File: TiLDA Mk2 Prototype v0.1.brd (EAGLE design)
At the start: 67.9 x 100 mm, 199 parts, among them IC1 ATSAM3X8EA-AU, IC10 MCP73831, IC2 MPU-6050, IC3 SRF-V1.2, IC5 S25FL216K0PMFI011, IC7 HMC5883LSMD (NP), IC8 MCP1825T-3302E/DC, IC9 TC1015-3V3, J1 ZX62-AB-5PA(11), J3 Arduino Headers, J5 1050270001 (NP), J6 B016 - PowerPOD NCP1402 5V0, J7 SFV30R-2STE1HLF, J8 1x02 RA Pin, Q10 2N7002KW, Q11 BSS84W, Q12 2N7002KW, Q13 BSS84W, Q8 BSS84W, Q9 2N7002KW, U2 JHD12864-G13BSW-OUTLINE, X1 12Mhz 13pF 30ppm (7pf caps), X2 32.768Khz

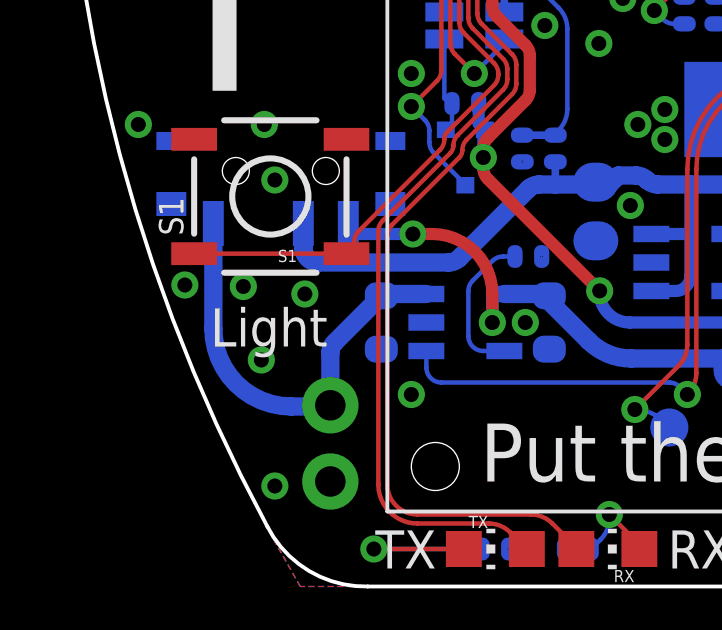
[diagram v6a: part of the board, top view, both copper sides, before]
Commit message: Prototype: Reverser polarity protection
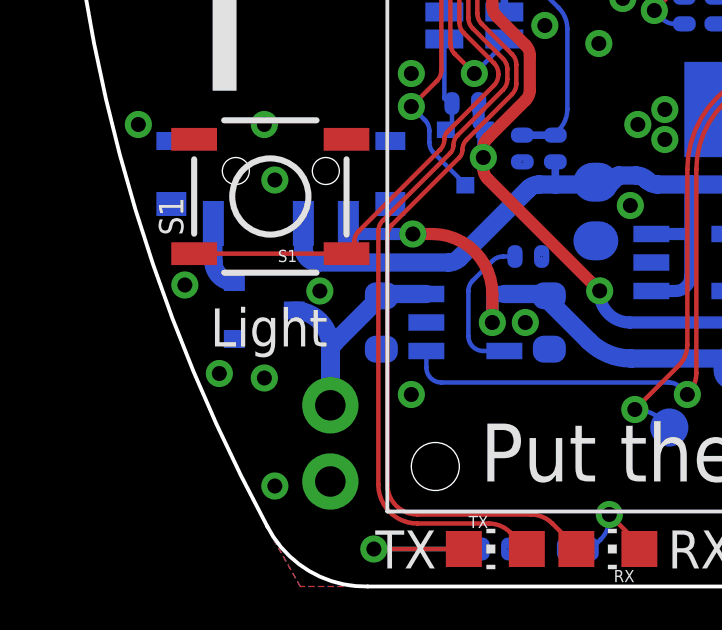
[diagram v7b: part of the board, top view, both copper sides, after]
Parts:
- added Q14: NTR1P02T1G, TiLDA Mk2 Parts:SOT23-R
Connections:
- new net VBATT_PROTECTED: Q14.2, S8.3
- net GND: now also Q14.1
- net VBATT: now also Q14.3; no longer S8.3
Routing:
- net VBATT: track 14.4 -> 9.50 mm
- net VBATT_PROTECTED: track 0.00 -> 2.24 mm
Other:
- board text added: "Q14"
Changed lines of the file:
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@@
 <text x="35.7" y="14.7" size="0.8128" layer="22" font="vector" ratio="15" rot="MR0">Accel</text>
 <text x="46.9" y="11.8" size="0.8128" layer="22" font="vector" ratio="15" rot="MR0">Compass</text>
+<text x="4.5" y="8.1" size="0.6096" layer="22" font="vector" ratio="15" rot="MR90">Q14</text>
 </plain>
 <attributes>
@@
 <attribute name="TP_SIGNAL_NAME" value="" x="20.3" y="5.3" size="1.778" layer="28" rot="MR0" display="off"/>
 </element>
+<element name="Q14" library="TiLDA Mk2 Parts" package="SOT23-R" value="NTR1P02T1G" x="6.8" y="9.2" rot="MR90"/>
 </elements>
 <signals>
@@
 <via x="11.4" y="20.4" extent="1-16" drill="0.5"/>
 <via x="11.7" y="17.1" extent="1-16" drill="0.5"/>
-<via x="6.1" y="10" extent="1-16" drill="0.5"/>
+<via x="5.3" y="7.1" extent="1-16" drill="0.5"/>
 <via x="11.5" y="39.9" extent="1-16" drill="0.5"/>
 <via x="11.35" y="42.1" extent="1-16" drill="0.5"/>
@@
 <via x="23.45" y="15.9" extent="1-16" drill="0.5"/>
 <via x="31.8" y="6.25" extent="1-16" drill="0.5"/>
-<via x="8.15" y="9.75" extent="1-16" drill="0.5"/>
+<via x="8.65" y="9.85" extent="1-16" drill="0.5"/>
 <via x="7.15" y="13.55" extent="1-16" drill="0.5"/>
 <via x="4.15" y="10.05" extent="1-16" drill="0.5"/>
@@
 <via x="66.05" y="61.95" extent="1-16" drill="0.5"/>
 <via x="63.95" y="53.75" extent="1-16" drill="0.5"/>
-<via x="6.7" y="7.55" extent="1-16" drill="0.5"/>
+<via x="6.8" y="6.95" extent="1-16" drill="0.5"/>
 <via x="15.5" y="8.8" extent="1-16" drill="0.5"/>
 <via x="60.75" y="13.6" extent="1-16" drill="0.5"/>
@@
 <via x="17.75" y="76.55" extent="1-16" drill="0.5"/>
 <via x="55.45" y="41.6" extent="1-16" drill="0.5"/>
+<contactref element="Q14" pad="1"/>
 </signal>
 <signal name="LCD_!CS">
@@
 </signal>
 <signal name="VBATT">
-<contactref element="S8" pad="3"/>
-<wire x1="5.1" y1="12.1" x2="5.1" y2="8.6" width="0.6096" layer="16"/>
 <contactref element="J8" pad="2"/>
 <contactref element="IC10" pad="3"/>
 <contactref element="C48" pad="2"/>
-<wire x1="5.1" y1="8.6" x2="7.7" y2="6" width="0.6096" layer="16" curve="90"/>
-<wire x1="7.7" y1="6" x2="9" y2="6" width="0.6096" layer="16"/>
 <wire x1="10.7" y1="9.689" x2="10.761" y2="9.75" width="0.4064" layer="16"/>
 <wire x1="10.761" y1="9.75" x2="12.1999" y2="9.75" width="0.6096" layer="16"/>
@@
 <wire x1="9.146446875" y1="8.135446875" x2="9" y2="7.78189375" width="0.6096" layer="16" curve="45"/>
 <wire x1="9" y1="7.78189375" x2="9" y2="6.04" width="0.6096" layer="16"/>
-<wire x1="9" y1="6" x2="9" y2="6.04" width="0.4064" layer="16"/>
+<contactref element="Q14" pad="3"/>
+<wire x1="7.8" y1="9.2" x2="9" y2="8" width="0.6096" layer="16" curve="-90"/>
+<wire x1="9" y1="8" x2="9" y2="6.04" width="0.6096" layer="16"/>
 </signal>
 <signal name="F1">
@@
 <wire x1="18.00710625" y1="1.56260625" x2="17.6945" y2="1.25" width="0.15" layer="16"/>
 </signal>
+<signal name="VBATT_PROTECTED">
+<contactref element="Q14" pad="2"/>
+<contactref element="S8" pad="3"/>
+<wire x1="5.8" y1="10.15" x2="5.1" y2="10.85" width="0.6096" layer="16" curve="-90"/>
+<wire x1="5.1" y1="10.85" x2="5.1" y2="12.1" width="0.6096" layer="16"/>
+</signal>
 </signals>

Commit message: Prototype: Minor schematic tweaks, board tweaks
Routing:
- net GND: vias 239 -> 241
